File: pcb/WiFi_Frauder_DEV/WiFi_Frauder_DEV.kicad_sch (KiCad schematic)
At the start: 8 parts, among them SW1 BTN_DOWN, SW2 BTN_UP, SW3 BTN_ENTER, U1 ESP32-DevKitC, U2 DM-OLED096-636

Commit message: feat: revision PCB from 0 to 1
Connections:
- net BTN_DOWN_NET: now reaches R1.2, SW1.1, U1.37 (GPIO23)
- net BTN_UP_NET: now reaches R2.2, SW2.1, U1.36 (GPIO22)
- net BTN_ENTER_NET: now reaches R3.2, SW3.1, U1.33 (GPIO21)
- net SCL renamed OLED_SCL_NET
- net SDA renamed OLED_SDA_NET
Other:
- note added: "DOWN BUTTON"
- note added: "ENTER BUTTON"
- note added: "UP BUTTON"
- moved on the sheet: R1, R2, R3, SW1, SW2, SW3, U1

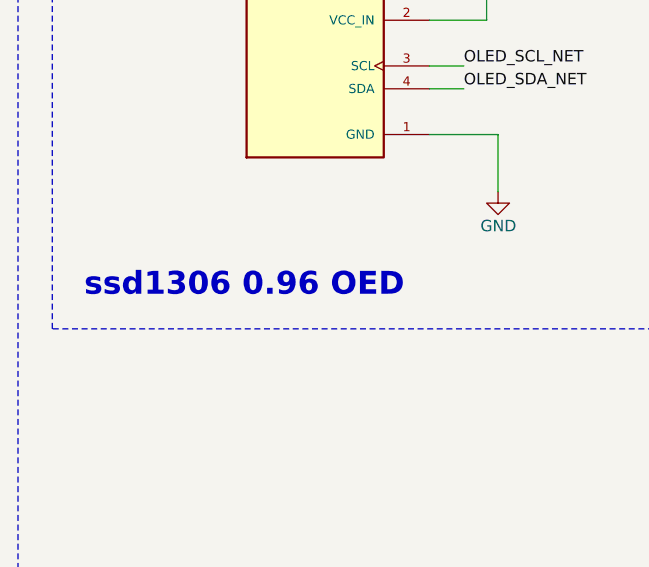
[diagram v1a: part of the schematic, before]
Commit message: fix: schema typo
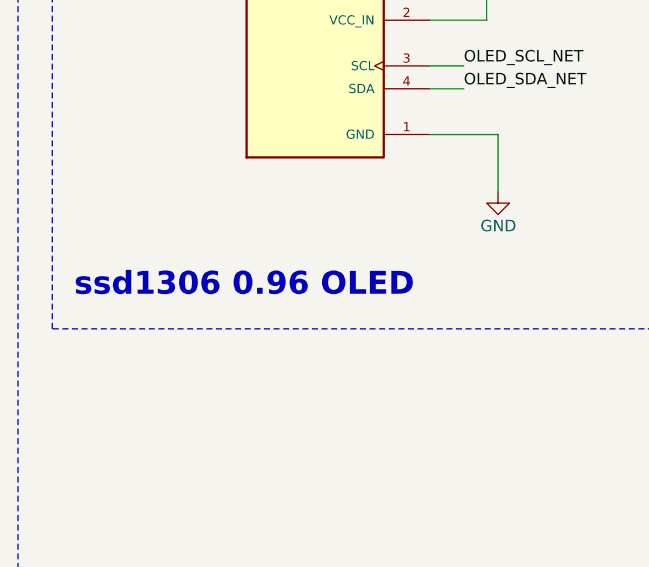
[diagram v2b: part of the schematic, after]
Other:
- note added: "ssd1306 0.96 OLED"
- note removed: "ssd1306 0.96 OED"
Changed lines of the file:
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@@
 		)
 	)
-	(text "ssd1306 0.96 OED "
+	(text "ssd1306 0.96 OLED "
 		(exclude_from_sim no)
 		(at 45.466 75.184 0)

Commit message: feat: revistion pcb to rev2
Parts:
- R1, R2, R3: footprint Capacitor_SMD:C_0805_2012Metric -> Resistor_THT:R_Axial_DIN0207_L6.3mm_D2.5mm_P10.16mm_Horizontal
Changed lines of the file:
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@@
 			)
 		)
-		(property "Footprint" "Capacitor_SMD:C_0805_2012Metric"
+		(property "Footprint" "Resistor_THT:R_Axial_DIN0207_L6.3mm_D2.5mm_P10.16mm_Horizontal"
 			(at 229.362 50.8 90)
 			(effects
@@
 			)
 		)
-		(property "Footprint" "Capacitor_SMD:C_0805_2012Metric"
+		(property "Footprint" "Resistor_THT:R_Axial_DIN0207_L6.3mm_D2.5mm_P10.16mm_Horizontal"
 			(at 221.742 88.9 90)
 			(effects
@@
 			)
 		)
-		(property "Footprint" "Capacitor_SMD:C_0805_2012Metric"
+		(property "Footprint" "Resistor_THT:R_Axial_DIN0207_L6.3mm_D2.5mm_P10.16mm_Horizontal"
 			(at 221.742 121.92 90)
 			(effects

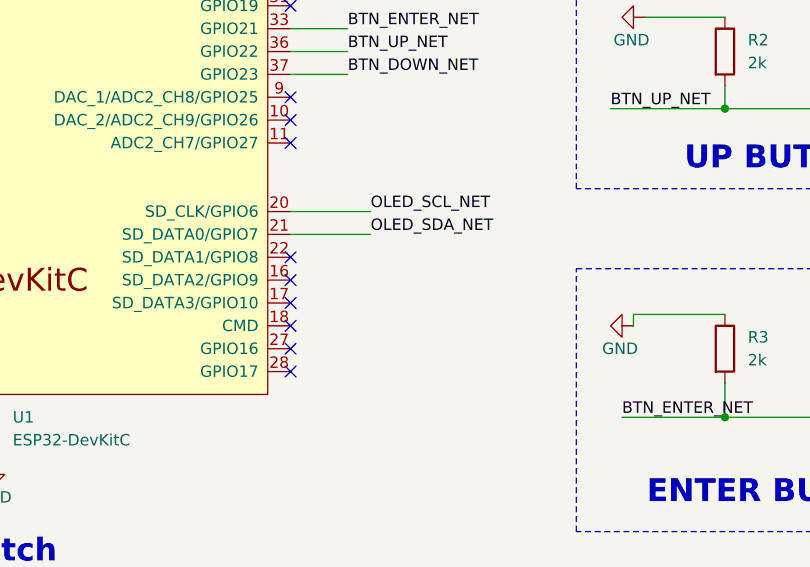
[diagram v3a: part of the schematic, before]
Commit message: fix: correct schema pinout; remove strapping pin
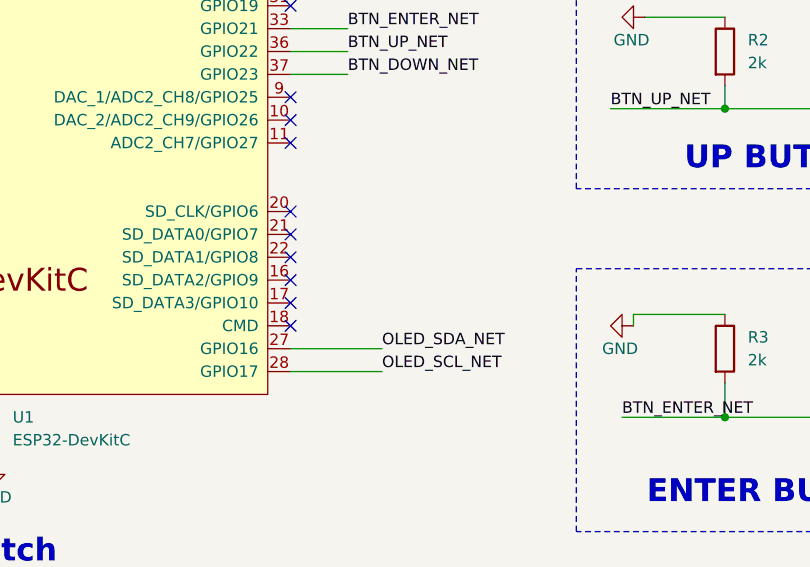
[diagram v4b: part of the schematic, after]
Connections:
- net OLED_SCL_NET: now also U1.28 (GPIO17); no longer U1.20 (SD_CLK/GPIO6)
- net OLED_SDA_NET: now also U1.27 (GPIO16); no longer U1.21 (SD_DATA0/GPIO7)
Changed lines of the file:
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@@
 	(title_block
 		(title "WiFi Frauder DEV")
-		(date "2025-06-10")
-		(rev "1")
+		(date "2025-06-14")
+		(rev "2")
 		(company "By Anuwat Khongchuai (un4ckn0wl3z)")
 	)
@@
 	)
 	(no_connect
+		(at 175.26 106.68)
+	)
+	(no_connect
 		(at 109.22 83.82)
 	)
@@
 	)
 	(no_connect
-		(at 175.26 124.46)
-	)
-	(no_connect
 		(at 144.78 58.42)
 	)
@@
 	)
 	(no_connect
-		(at 175.26 121.92)
-	)
-	(no_connect
 		(at 175.26 111.76)
 	)
@@
 	)
 	(no_connect
+		(at 175.26 109.22)
+	)
+	(no_connect
 		(at 175.26 119.38)
 	)
@@
 	(wire
 		(pts
-			(xy 175.26 106.68) (xy 184.15 106.68)
-		)
-		(stroke
-			(width 0)
-			(type default)
-		)
-	)
-	(wire
-		(pts
 			(xy 214.63 85.09) (xy 223.52 85.09)
 		)
@@
 	(wire
 		(pts
+			(xy 185.42 121.92) (xy 175.26 121.92)
+		)
+		(stroke
+			(width 0)
+			(type default)
+		)
+	)
+	(wire
+		(pts
 			(xy 175.26 86.36) (xy 181.61 86.36)
 		)
@@
 	(wire
 		(pts
-			(xy 175.26 109.22) (xy 184.15 109.22)
-		)
-		(stroke
-			(width 0)
-			(type default)
-		)
-	)
-	(wire
-		(pts
 			(xy 252.73 58.42) (xy 267.97 58.42)
 		)
@@
 		(pts
 			(xy 242.57 58.42) (xy 231.14 58.42)
+		)
+		(stroke
+			(width 0)
+			(type default)
+		)
+	)
+	(wire
+		(pts
+			(xy 185.42 124.46) (xy 175.26 124.46)
 		)
 		(stroke
@@
 		)
 	)
-	(label "OLED_SDA_NET"
-		(at 184.15 109.22 0)
-		(effects
-			(font
-				(size 1.27 1.27)
-			)
-			(justify left bottom)
-		)
-	)
 	(label "BTN_DOWN_NET"
 		(at 213.36 58.42 0)
@@
 		)
 	)
-	(label "OLED_SCL_NET"
-		(at 184.15 106.68 0)
-		(effects
-			(font
-				(size 1.27 1.27)
-			)
-			(justify left bottom)
-		)
-	)
 	(label "OLED_SDA_NET"
 		(at 69.85 53.34 0)
@@
 		(effects
 			(font
+				(size 1.27 1.27)
+			)
+			(justify left bottom)
+		)
+	)
+	(label "OLED_SDA_NET"
+		(at 185.42 121.92 0)
+		(effects
+			(font
+				(size 1.27 1.27)
+			)
+			(justify left bottom)
+		)
+	)
+	(label "OLED_SCL_NET"
+		(at 185.42 124.46 0)
+		(effects
+			(font

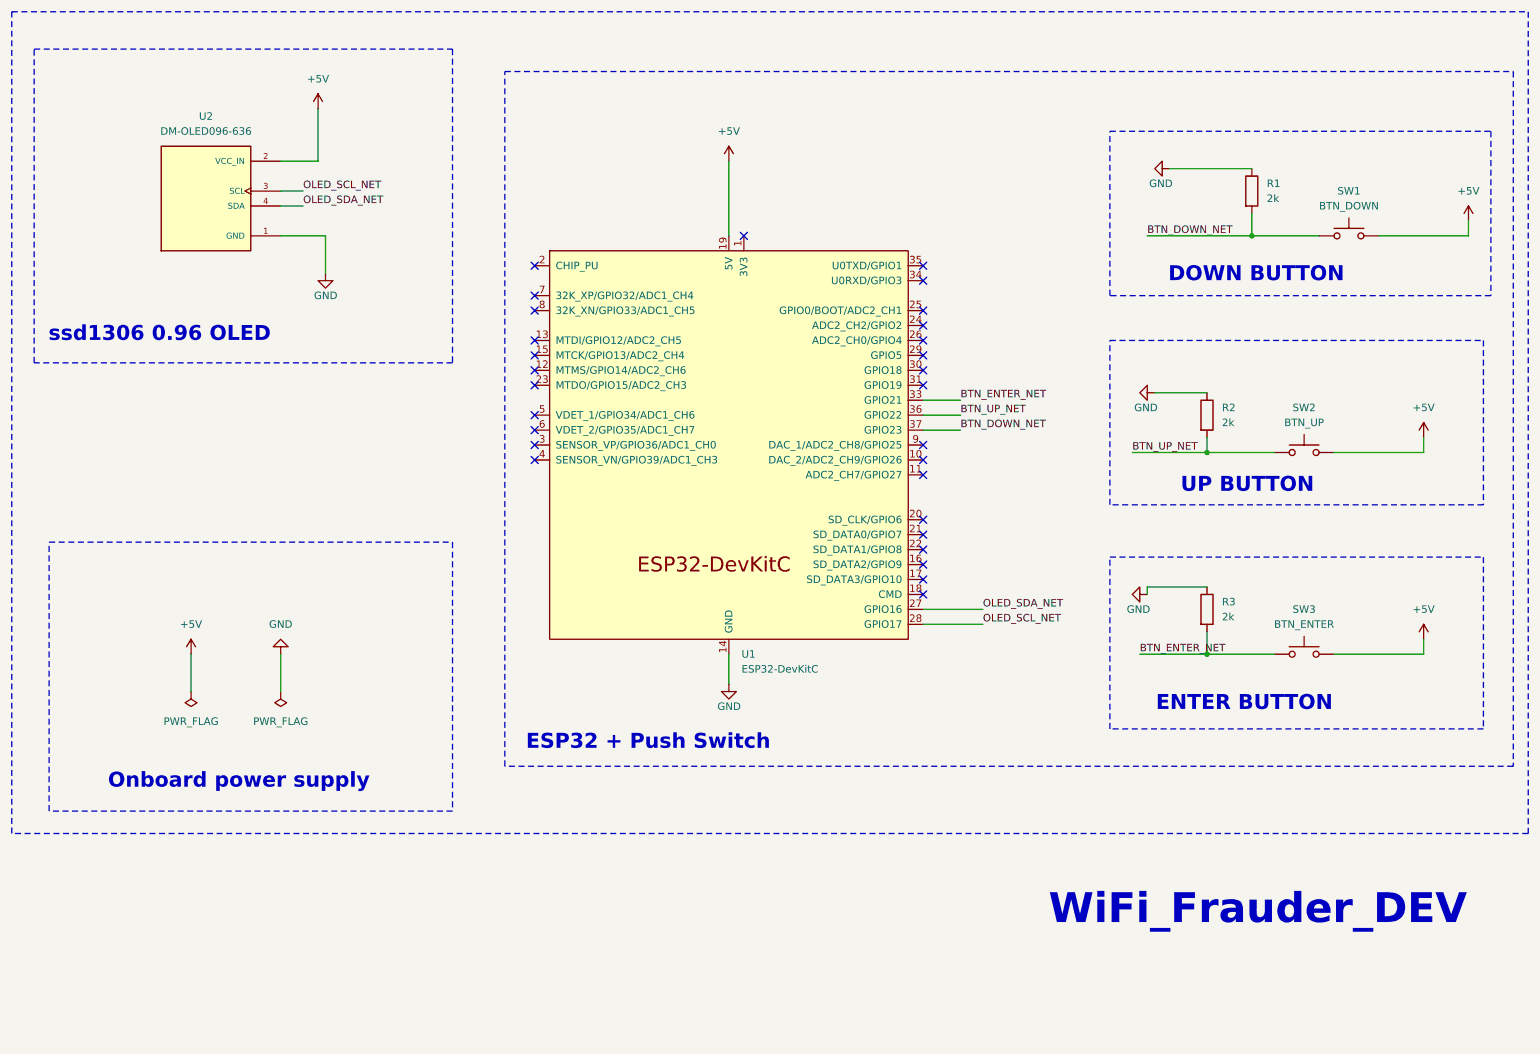
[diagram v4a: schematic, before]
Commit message: feat: re-designed pcb included extended female socket for GPIO
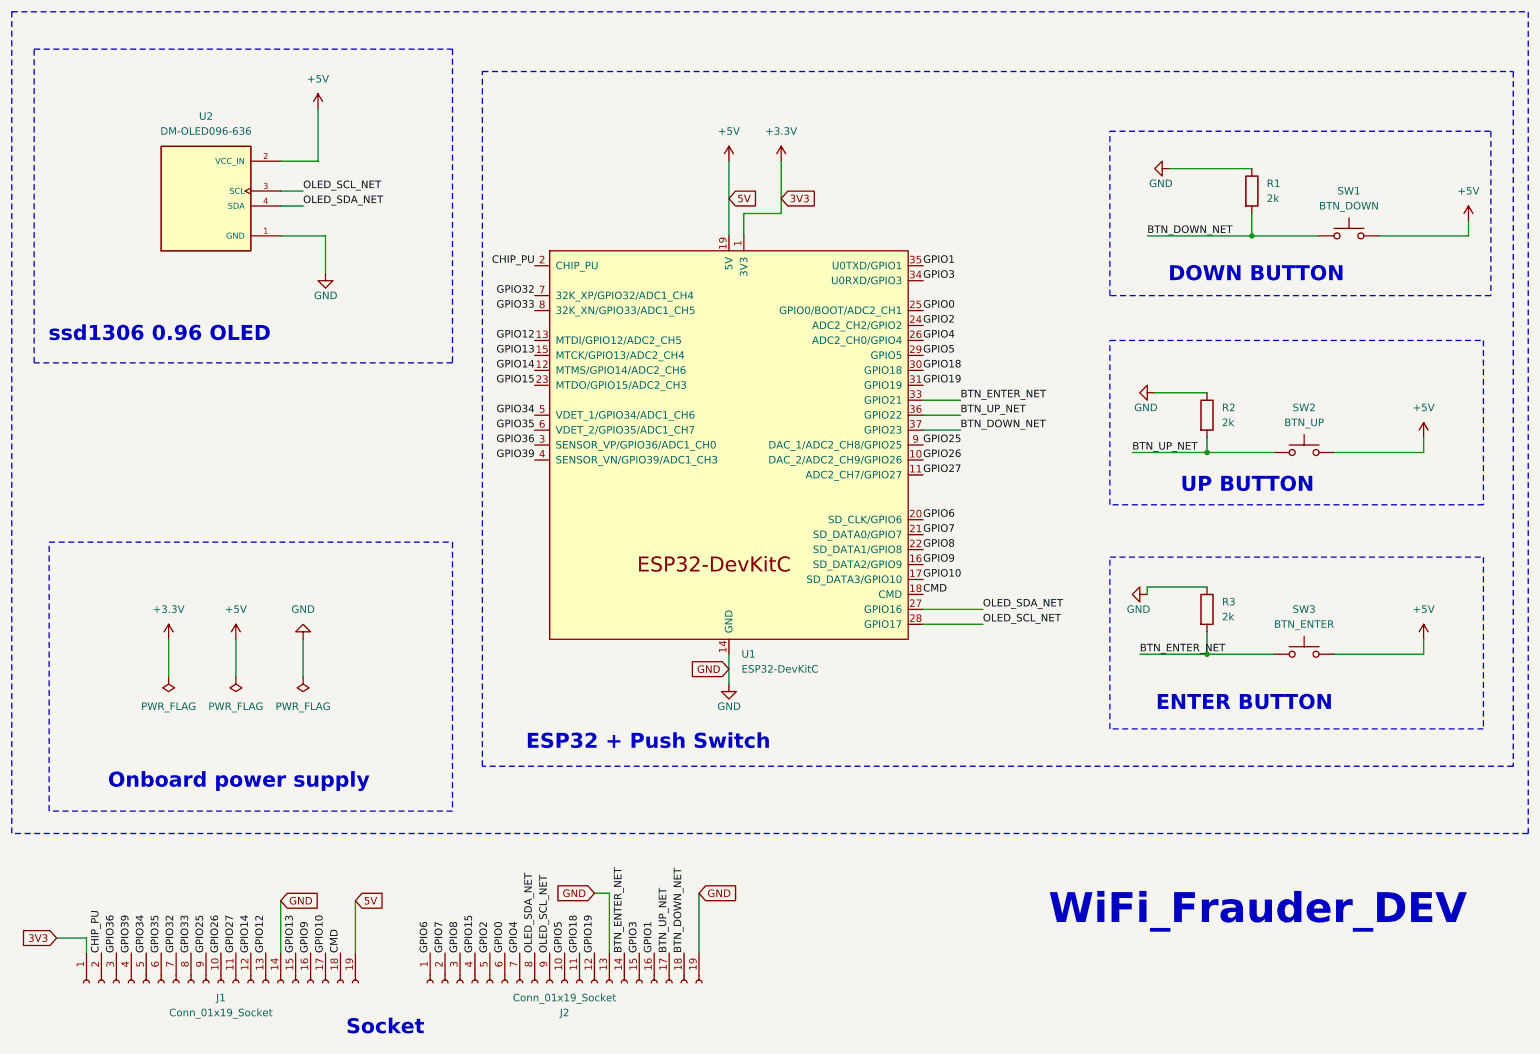
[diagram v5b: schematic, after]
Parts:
- added J1, J2: Conn_01x19_Socket, Connector_PinSocket_2.54mm:PinSocket_1x19_P2.54mm_Vertical, symbol Connector:Conn_01x19_Socket
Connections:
- net +5V: now also J1.19 (Pin_19)
- net BTN_DOWN_NET: now also J2.18 (Pin_18)
- net BTN_ENTER_NET: now also J2.14 (Pin_14)
- net BTN_UP_NET: now also J2.17 (Pin_17)
- net GND: now also J1.14 (Pin_14), J2.13 (Pin_13), J2.19 (Pin_19)
- net OLED_SCL_NET: now also J2.9 (Pin_9)
- net OLED_SDA_NET: now also J2.8 (Pin_8)
- net +3.3V: now reaches U1.1 (3V3)
- net +3.3V: now also J1.1 (Pin_1)
- net GPIO26: now reaches U1.10 (DAC_2/ADC2_CH9/GPIO26)
- net GPIO26: now also J1.10 (Pin_10)
- net GPIO27: now reaches U1.11 (ADC2_CH7/GPIO27)
- net GPIO27: now also J1.11 (Pin_11)
- net GPIO14: now reaches U1.12 (MTMS/GPIO14/ADC2_CH6)
- net GPIO14: now also J1.12 (Pin_12)
- net GPIO12: now reaches U1.13 (MTDI/GPIO12/ADC2_CH5)
- net GPIO12: now also J1.13 (Pin_13)
- net GPIO13: now reaches U1.15 (MTCK/GPIO13/ADC2_CH4)
- net GPIO13: now also J1.15 (Pin_15)
- net GPIO9: now reaches U1.16 (SD_DATA2/GPIO9)
- net GPIO9: now also J1.16 (Pin_16)
- net GPIO10: now reaches U1.17 (SD_DATA3/GPIO10)
- net GPIO10: now also J1.17 (Pin_17)
- net CMD: now reaches U1.18 (CMD)
- net CMD: now also J1.18 (Pin_18)
- net CHIP_PU: now reaches U1.2 (CHIP_PU)
- net CHIP_PU: now also J1.2 (Pin_2)
- net GPIO6: now reaches U1.20 (SD_CLK/GPIO6)
- net GPIO6: now also J2.1 (Pin_1)
- net GPIO7: now reaches U1.21 (SD_DATA0/GPIO7)
- net GPIO7: now also J2.2 (Pin_2)
- net GPIO8: now reaches U1.22 (SD_DATA1/GPIO8)
- net GPIO8: now also J2.3 (Pin_3)
- net GPIO15: now reaches U1.23 (MTDO/GPIO15/ADC2_CH3)
- net GPIO15: now also J2.4 (Pin_4)
- net GPIO2: now reaches U1.24 (ADC2_CH2/GPIO2)
- net GPIO2: now also J2.5 (Pin_5)
- net GPIO0: now reaches U1.25 (GPIO0/BOOT/ADC2_CH1)
- net GPIO0: now also J2.6 (Pin_6)
- net GPIO4: now reaches U1.26 (ADC2_CH0/GPIO4)
- net GPIO4: now also J2.7 (Pin_7)
- net GPIO5: now reaches U1.29 (GPIO5)
- net GPIO5: now also J2.10 (Pin_10)
- net GPIO36: now reaches U1.3 (SENSOR_VP/GPIO36/ADC1_CH0)
- net GPIO36: now also J1.3 (Pin_3)
- net GPIO18: now reaches U1.30 (GPIO18)
- net GPIO18: now also J2.11 (Pin_11)
- net GPIO19: now reaches U1.31 (GPIO19)
- net GPIO19: now also J2.12 (Pin_12)
- net GPIO3: now reaches U1.34 (U0RXD/GPIO3)
- net GPIO3: now also J2.15 (Pin_15)
- net GPIO1: now reaches U1.35 (U0TXD/GPIO1)
- net GPIO1: now also J2.16 (Pin_16)
- net GPIO39: now reaches U1.4 (SENSOR_VN/GPIO39/ADC1_CH3)
- net GPIO39: now also J1.4 (Pin_4)
- net GPIO34: now reaches U1.5 (VDET_1/GPIO34/ADC1_CH6)
- net GPIO34: now also J1.5 (Pin_5)
- net GPIO35: now reaches U1.6 (VDET_2/GPIO35/ADC1_CH7)
- net GPIO35: now also J1.6 (Pin_6)
- net GPIO32: now reaches U1.7 (32K_XP/GPIO32/ADC1_CH4)
- net GPIO32: now also J1.7 (Pin_7)
- net GPIO33: now reaches U1.8 (32K_XN/GPIO33/ADC1_CH5)
- net GPIO33: now also J1.8 (Pin_8)
- net GPIO25: now reaches U1.9 (DAC_1/ADC2_CH8/GPIO25)
- net GPIO25: now also J1.9 (Pin_9)
- no-connect marks 29 -> 0
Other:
- note added: "Socket"
